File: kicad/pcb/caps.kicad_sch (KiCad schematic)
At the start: 58 parts

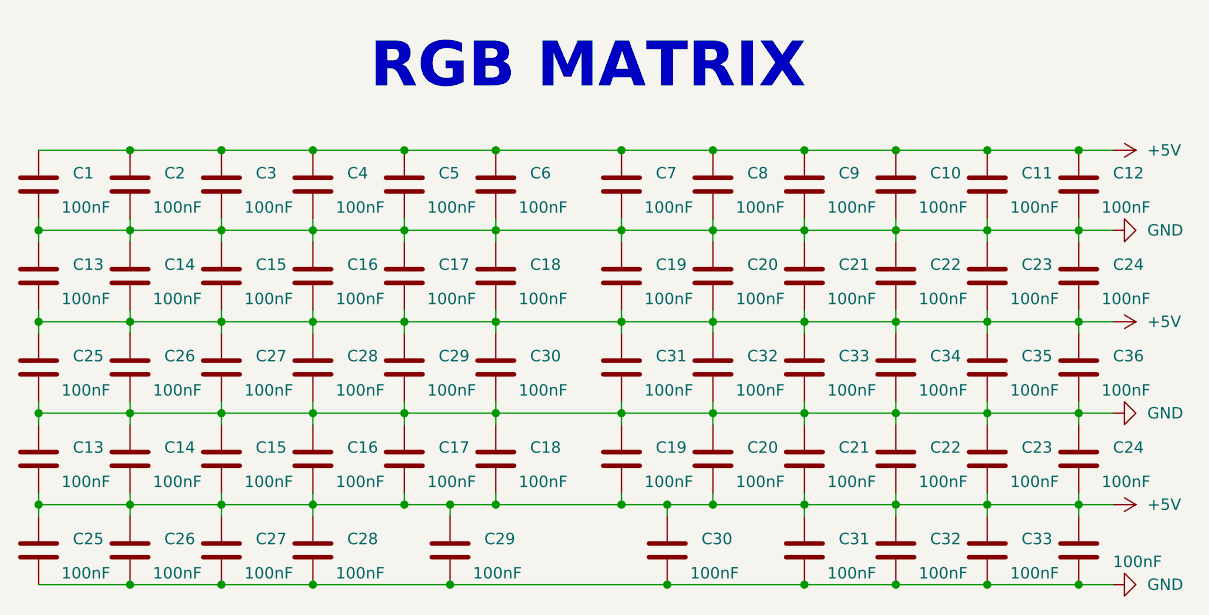
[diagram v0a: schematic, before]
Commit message: USB (almost) done + some STM progress
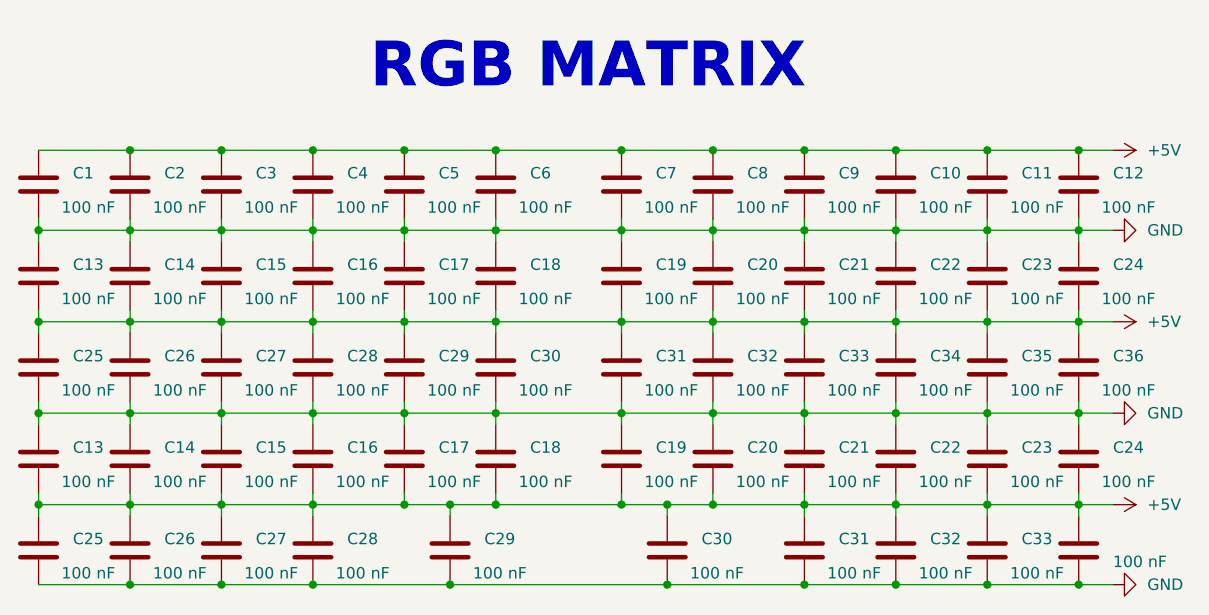
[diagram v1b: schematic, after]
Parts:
- C1, C10, C11, C12, C13, C14, C15, C16, C17, C18, C19, C2, C20, C21, C22, C23, C24, C25, C26, C27, C28, C29, C3, C30, C31, C32, C33, C34, C35, C36, C4, C5, C6, C7, C8, C9: value 100nF -> 100 nF

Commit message: Initial support circuitry for STM and ESP
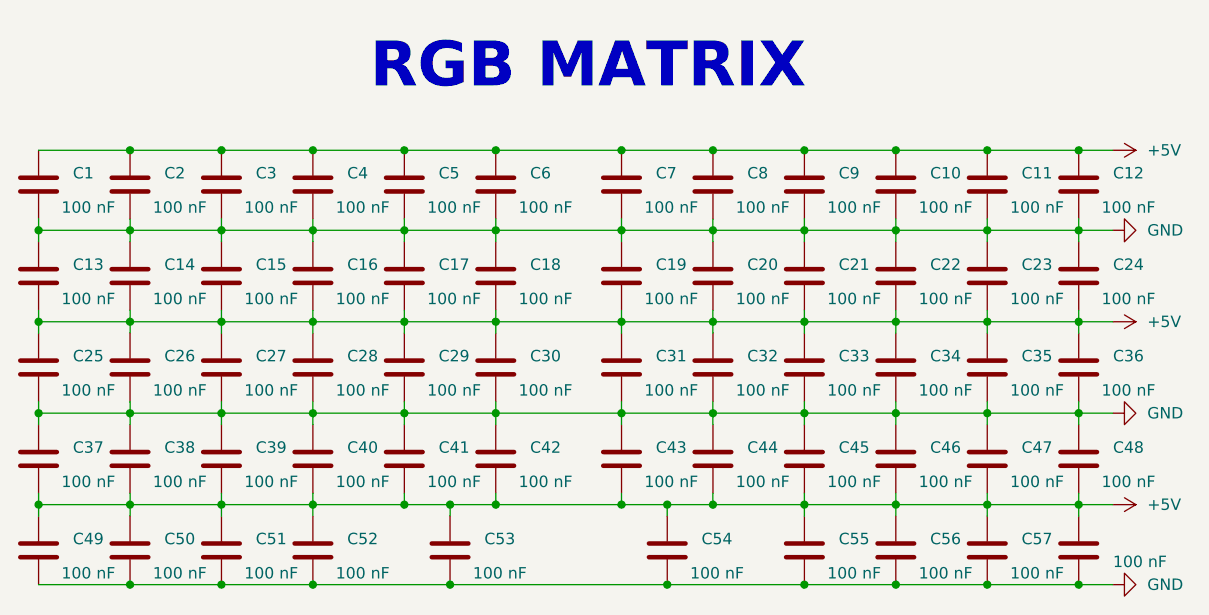
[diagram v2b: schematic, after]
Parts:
- renumbered C13 to C37, C14 to C38, C15 to C39, C16 to C40, C17 to C41, C18 to C42, C19 to C43, C20 to C44, C21 to C45, C22 to C46, C23 to C47, C24 to C48, C25 to C49, C26 to C50, C27 to C51, C28 to C52, C29 to C53, C30 to C54, C31 to C55, C32 to C56, C33 to C57, C34 to C58
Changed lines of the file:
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@@
   (symbol (lib_id "Device:C") (at 69.85 72.39 0) (unit 1)
     (in_bom yes) (on_board yes) (dnp no)
-    (property "Reference" "C29" (at 73.66 71.12 0)
+    (property "Reference" "C53" (at 73.66 71.12 0)
       (effects (font (size 1.27 1.27)) (justify left))
     )
@@
   (symbol (lib_id "Device:C") (at 34.29 62.23 0) (unit 1)
     (in_bom yes) (on_board yes) (dnp no)
-    (property "Reference" "C14" (at 38.1 60.96 0)
+    (property "Reference" "C38" (at 38.1 60.96 0)
       (effects (font (size 1.27 1.27)) (justify left))
     )
@@
   (symbol (lib_id "power:GND") (at 143.51 57.15 90) (unit 1)
     (in_bom yes) (on_board yes) (dnp no) (fields_autoplaced)
-    (property "Reference" "#PWR010" (at 149.86 57.15 0)
+    (property "Reference" "#PWR05" (at 149.86 57.15 0)
       (effects (font (size 1.27 1.27)) hide)
     )
@@
   (symbol (lib_id "Device:C") (at 119.38 62.23 0) (unit 1)
     (in_bom yes) (on_board yes) (dnp no)
-    (property "Reference" "C22" (at 123.19 60.96 0)
+    (property "Reference" "C46" (at 123.19 60.96 0)
       (effects (font (size 1.27 1.27)) (justify left))
     )
@@
   (symbol (lib_id "Device:C") (at 129.54 62.23 0) (unit 1)
     (in_bom yes) (on_board yes) (dnp no)
-    (property "Reference" "C23" (at 133.35 60.96 0)
+    (property "Reference" "C47" (at 133.35 60.96 0)
       (effects (font (size 1.27 1.27)) (justify left))
     )
@@
   (symbol (lib_id "Device:C") (at 24.13 62.23 0) (unit 1)
     (in_bom yes) (on_board yes) (dnp no)
-    (property "Reference" "C13" (at 27.94 60.96 0)
+    (property "Reference" "C37" (at 27.94 60.96 0)
       (effects (font (size 1.27 1.27)) (justify left))
     )
@@
   (symbol (lib_id "Device:C") (at 139.7 72.39 0) (unit 1)
     (in_bom yes) (on_board yes) (dnp no) (fields_autoplaced)
-    (property "Reference" "C34" (at 143.51 71.12 0)
+    (property "Reference" "C58" (at 143.51 71.12 0)
       (effects (font (size 1.27 1.27)) (justify left) hide)
     )
@@
   (symbol (lib_id "Device:C") (at 109.22 62.23 0) (unit 1)
     (in_bom yes) (on_board yes) (dnp no)
-    (property "Reference" "C21" (at 113.03 60.96 0)
+    (property "Reference" "C45" (at 113.03 60.96 0)
       (effects (font (size 1.27 1.27)) (justify left))
     )
@@
   (symbol (lib_id "power:+5V") (at 143.51 67.31 270) (unit 1)
     (in_bom yes) (on_board yes) (dnp no) (fields_autoplaced)
-    (property "Reference" "#PWR03" (at 139.7 67.31 0)
+    (property "Reference" "#PWR06" (at 139.7 67.31 0)
       (effects (font (size 1.27 1.27)) hide)
     )
@@
   (symbol (lib_id "power:GND") (at 143.51 76.2 90) (unit 1)
     (in_bom yes) (on_board yes) (dnp no) (fields_autoplaced)
-    (property "Reference" "#PWR012" (at 149.86 76.2 0)
+    (property "Reference" "#PWR07" (at 149.86 76.2 0)
       (effects (font (size 1.27 1.27)) hide)
     )
@@
   (symbol (lib_id "Device:C") (at 93.98 72.39 0) (unit 1)
     (in_bom yes) (on_board yes) (dnp no)
-    (property "Reference" "C30" (at 97.79 71.12 0)
+    (property "Reference" "C54" (at 97.79 71.12 0)
       (effects (font (size 1.27 1.27)) (justify left))
     )
@@
   (symbol (lib_id "Device:C") (at 44.45 62.23 0) (unit 1)
     (in_bom yes) (on_board yes) (dnp no)
-    (property "Reference" "C15" (at 48.26 60.96 0)
+    (property "Reference" "C39" (at 48.26 60.96 0)
       (effects (font (size 1.27 1.27)) (justify left))
     )
@@
   (symbol (lib_id "Device:C") (at 139.7 62.23 0) (unit 1)
     (in_bom yes) (on_board yes) (dnp no)
-    (property "Reference" "C24" (at 143.51 60.96 0)
+    (property "Reference" "C48" (at 143.51 60.96 0)
       (effects (font (size 1.27 1.27)) (justify left))
     )
@@
   (symbol (lib_id "Device:C") (at 74.93 62.23 0) (unit 1)
     (in_bom yes) (on_board yes) (dnp no)
-    (property "Reference" "C18" (at 78.74 60.96 0)
+    (property "Reference" "C42" (at 78.74 60.96 0)
       (effects (font (size 1.27 1.27)) (justify left))
     )
@@
   (symbol (lib_id "Device:C") (at 119.38 72.39 0) (unit 1)
     (in_bom yes) (on_board yes) (dnp no)
-    (property "Reference" "C32" (at 123.19 71.12 0)
+    (property "Reference" "C56" (at 123.19 71.12 0)
       (effects (font (size 1.27 1.27)) (justify left))
     )
@@
   (symbol (lib_id "Device:C") (at 44.45 72.39 0) (unit 1)
     (in_bom yes) (on_board yes) (dnp no)
-    (property "Reference" "C27" (at 48.26 71.12 0)
+    (property "Reference" "C51" (at 48.26 71.12 0)
       (effects (font (size 1.27 1.27)) (justify left))
     )
@@
   (symbol (lib_id "power:+5V") (at 143.51 27.94 270) (unit 1)
     (in_bom yes) (on_board yes) (dnp no) (fields_autoplaced)
-    (property "Reference" "#PWR03" (at 139.7 27.94 0)
+    (property "Reference" "#PWR02" (at 139.7 27.94 0)
       (effects (font (size 1.27 1.27)) hide)
     )
@@
   (symbol (lib_id "Device:C") (at 129.54 72.39 0) (unit 1)
     (in_bom yes) (on_board yes) (dnp no)
-    (property "Reference" "C33" (at 133.35 71.12 0)
+    (property "Reference" "C57" (at 133.35 71.12 0)
       (effects (font (size 1.27 1.27)) (justify left))
     )
@@
   (symbol (lib_id "power:GND") (at 143.51 36.83 90) (unit 1)
     (in_bom yes) (on_board yes) (dnp no) (fields_autoplaced)
-    (property "Reference" "#PWR08" (at 149.86 36.83 0)
+    (property "Reference" "#PWR03" (at 149.86 36.83 0)
       (effects (font (size 1.27 1.27)) hide)
     )
@@
   (symbol (lib_id "Device:C") (at 34.29 72.39 0) (unit 1)
     (in_bom yes) (on_board yes) (dnp no)
-    (property "Reference" "C26" (at 38.1 71.12 0)
+    (property "Reference" "C50" (at 38.1 71.12 0)
       (effects (font (size 1.27 1.27)) (justify left))
     )
@@
   (symbol (lib_id "Device:C") (at 88.9 62.23 0) (unit 1)
     (in_bom yes) (on_board yes) (dnp no)
-    (property "Reference" "C19" (at 92.71 60.96 0)
+    (property "Reference" "C43" (at 92.71 60.96 0)
       (effects (font (size 1.27 1.27)) (justify left))
     )
@@
   (symbol (lib_id "Device:C") (at 99.06 62.23 0) (unit 1)
     (in_bom yes) (on_board yes) (dnp no)
-    (property "Reference" "C20" (at 102.87 60.96 0)
+    (property "Reference" "C44" (at 102.87 60.96 0)
       (effects (font (size 1.27 1.27)) (justify left))
     )
@@
   (symbol (lib_id "Device:C") (at 54.61 62.23 0) (unit 1)
     (in_bom yes) (on_board yes) (dnp no)
-    (property "Reference" "C16" (at 58.42 60.96 0)
+    (property "Reference" "C40" (at 58.42 60.96 0)
       (effects (font (size 1.27 1.27)) (justify left))
     )
@@
   (symbol (lib_id "Device:C") (at 54.61 72.39 0) (unit 1)
     (in_bom yes) (on_board yes) (dnp no)
-    (property "Reference" "C28" (at 58.42 71.12 0)
+    (property "Reference" "C52" (at 58.42 71.12 0)
       (effects (font (size 1.27 1.27)) (justify left))
     )
@@
   (symbol (lib_id "power:+5V") (at 143.51 46.99 270) (unit 1)
     (in_bom yes) (on_board yes) (dnp no) (fields_autoplaced)
-    (property "Reference" "#PWR03" (at 139.7 46.99 0)
+    (property "Reference" "#PWR04" (at 139.7 46.99 0)
       (effects (font (size 1.27 1.27)) hide)
     )
@@
   (symbol (lib_id "Device:C") (at 109.22 72.39 0) (unit 1)
     (in_bom yes) (on_board yes) (dnp no)
-    (property "Reference" "C31" (at 113.03 71.12 0)
+    (property "Reference" "C55" (at 113.03 71.12 0)
       (effects (font (size 1.27 1.27)) (justify left))
     )
@@
   (symbol (lib_id "Device:C") (at 24.13 72.39 0) (unit 1)
     (in_bom yes) (on_board yes) (dnp no)
-    (property "Reference" "C25" (at 27.94 71.12 0)
+    (property "Reference" "C49" (at 27.94 71.12 0)
       (effects (font (size 1.27 1.27)) (justify left))
     )
@@
   (symbol (lib_id "Device:C") (at 64.77 62.23 0) (unit 1)
     (in_bom yes) (on_board yes) (dnp no)
-    (property "Reference" "C17" (at 68.58 60.96 0)
-      (effects (font (size 1.27 1.27)) (justify left))
-    )
+    (property "Reference" "C41" (at 68.58 60.96 0)
+      (effects (font (size 1.27 1.27)) (justify left))
+    )

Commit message: Hub wired(?) + STM and ESP may boot already
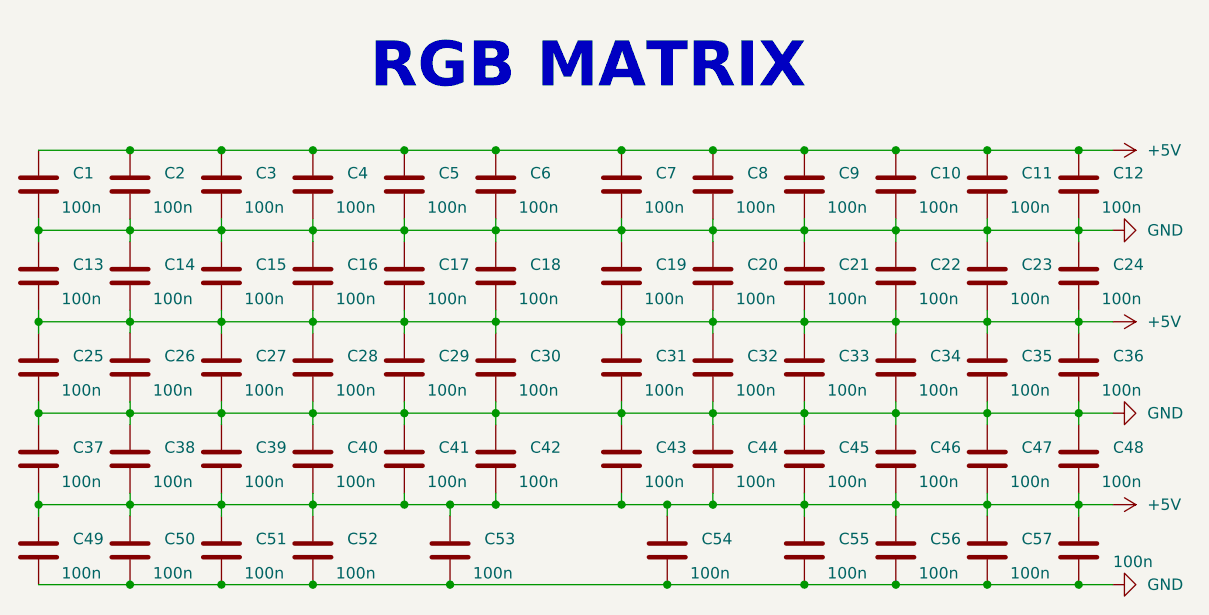
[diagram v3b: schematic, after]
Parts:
- C1, C10, C11, C12, C13, C14, C15, C16, C17, C18, C19, C2, C20, C21, C22, C23, C24, C25, C26, C27, C28, C29, C3, C30, C31, C32, C33, C34, C35, C36, C37, C38, C39, C4, C40, C41, C42, C43, C44, C45, C46, C47, C48, C49, C5, C50, C51, C52, C53, C54, C55, C56, C57, C58, C6, C7, C8, C9: value 100 nF -> 100n

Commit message: (WIP) Tracing v2
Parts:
- C1, C10, C11, C12, C13, C14, C15, C16, C17, C18, C19, C2, C20, C21, C22, C23, C24, C25, C26, C27, C28, C29, C3, C30, C31, C32, C33, C34, C35, C36, C37, C38, C39, C4, C40, C41, C42, C43, C44, C45, C46, C47, C48, C49, C5, C50, C51, C52, C53, C54, C55, C56, C57, C58, C6, C7, C8, C9: footprint Capacitor_SMD:C_1206_3216Metric_Pad1.33x1.80mm_HandSolder -> Capacitor_SMD:C_0402_1005Metric_Pad0.74x0.62mm_HandSolder
